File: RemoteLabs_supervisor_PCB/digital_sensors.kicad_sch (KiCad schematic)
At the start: 8 parts

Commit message: V1.0 Circuit Design Complete
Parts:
- gave numbers to parts that had none: 8
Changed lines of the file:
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@@
   (symbol (lib_id "000_Resistors_Immo:Resistor_0805") (at 128.27 99.06 0) (unit 1)
     (in_bom yes) (on_board yes) (fields_autoplaced)
-    (property "Reference" "R?" (id 0) (at 130.81 97.7899 0)
+    (property "Reference" "R21" (id 0) (at 130.81 97.7899 0)
       (effects (font (size 1.27 1.27)) (justify left))
     )
@@
   (symbol (lib_id "000_Resistors_Immo:Resistor_0805") (at 101.6 99.06 0) (unit 1)
     (in_bom yes) (on_board yes) (fields_autoplaced)
-    (property "Reference" "R?" (id 0) (at 104.14 97.7899 0)
+    (property "Reference" "R17" (id 0) (at 104.14 97.7899 0)
       (effects (font (size 1.27 1.27)) (justify left))
     )
@@
   (symbol (lib_id "000_Resistors_Immo:Resistor_0805") (at 118.11 38.1 0) (unit 1)
     (in_bom yes) (on_board yes) (fields_autoplaced)
-    (property "Reference" "R?" (id 0) (at 120.65 36.8299 0)
+    (property "Reference" "R20" (id 0) (at 120.65 36.8299 0)
       (effects (font (size 1.27 1.27)) (justify left))
     )
@@
   (symbol (lib_id "000_Resistors_Immo:Resistor_0805") (at 114.3 99.06 0) (unit 1)
     (in_bom yes) (on_board yes) (fields_autoplaced)
-    (property "Reference" "R?" (id 0) (at 116.84 97.7899 0)
+    (property "Reference" "R19" (id 0) (at 116.84 97.7899 0)
       (effects (font (size 1.27 1.27)) (justify left))
     )
@@
   (symbol (lib_id "Connector:Conn_01x02_Male") (at 87.63 45.72 0) (unit 1)
     (in_bom yes) (on_board yes) (fields_autoplaced)
-    (property "Reference" "J?" (id 0) (at 88.265 40.64 0))
+    (property "Reference" "J23" (id 0) (at 88.265 40.64 0))
     (property "Value" "limit_switch_A" (id 1) (at 88.265 43.18 0))
     (property "Footprint" "" (id 2) (at 87.63 45.72 0)
@@
   (symbol (lib_id "000_Pin_Headers_Immo:Conn_01x05_Male") (at 87.63 106.68 0) (mirror x) (unit 1)
     (in_bom yes) (on_board yes)
-    (property "Reference" "J?" (id 0) (at 78.74 95.25 0))
+    (property "Reference" "J25" (id 0) (at 78.74 95.25 0))
     (property "Value" "Optical Encoder" (id 1) (at 85.09 97.79 0))
     (property "Footprint" "Connector_PinHeader_1.27mm:PinHeader_1x05_P1.27mm_Vertical" (id 2) (at 87.63 106.68 0)
@@
   (symbol (lib_id "000_Resistors_Immo:Resistor_0805") (at 110.49 38.1 0) (unit 1)
     (in_bom yes) (on_board yes) (fields_autoplaced)
-    (property "Reference" "R?" (id 0) (at 113.03 36.8299 0)
+    (property "Reference" "R18" (id 0) (at 113.03 36.8299 0)
       (effects (font (size 1.27 1.27)) (justify left))
     )
@@
   (symbol (lib_id "Connector:Conn_01x02_Male") (at 87.63 55.88 0) (unit 1)
     (in_bom yes) (on_board yes) (fields_autoplaced)
-    (property "Reference" "J?" (id 0) (at 88.265 50.8 0))
+    (property "Reference" "J24" (id 0) (at 88.265 50.8 0))
     (property "Value" "limit_switch_B" (id 1) (at 88.265 53.34 0))
     (property "Footprint" "" (id 2) (at 87.63 55.88 0)

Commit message: Schematic reviewed
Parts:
- J23, J24: footprint (none) -> Connector_PinHeader_2.54mm:PinHeader_1x02_P2.54mm_Vertical
- J25: footprint Connector_PinHeader_1.27mm:PinHeader_1x05_P1.27mm_Vertical -> Connector_PinHeader_2.54mm:PinHeader_1x05_P2.54mm_Vertical
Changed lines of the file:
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@@
     (property "Reference" "J23" (id 0) (at 88.265 40.64 0))
     (property "Value" "limit_switch_A" (id 1) (at 88.265 43.18 0))
-    (property "Footprint" "" (id 2) (at 87.63 45.72 0)
+    (property "Footprint" "Connector_PinHeader_2.54mm:PinHeader_1x02_P2.54mm_Vertical" (id 2) (at 87.63 45.72 0)
       (effects (font (size 1.27 1.27)) hide)
     )
@@
     (property "Reference" "J25" (id 0) (at 78.74 95.25 0))
     (property "Value" "Optical Encoder" (id 1) (at 85.09 97.79 0))
-    (property "Footprint" "Connector_PinHeader_1.27mm:PinHeader_1x05_P1.27mm_Vertical" (id 2) (at 87.63 106.68 0)
+    (property "Footprint" "Connector_PinHeader_2.54mm:PinHeader_1x05_P2.54mm_Vertical" (id 2) (at 87.63 106.68 0)
       (effects (font (size 1.27 1.27)) hide)
     )
@@
     (pin "2")
   )
-  (symbol (lib_id "Connector:Conn_01x02_Male") (at 87.63 55.88 0) (unit 1)
+  (symbol (lib_name "Conn_01x02_Male_1") (lib_id "Connector:Conn_01x02_Male") (at 87.63 55.88 0) (unit 1)
     (in_bom yes) (on_board yes) (fields_autoplaced)
     (property "Reference" "J24" (id 0) (at 88.265 50.8 0))
     (property "Value" "limit_switch_B" (id 1) (at 88.265 53.34 0))
-    (property "Footprint" "" (id 2) (at 87.63 55.88 0)
+    (property "Footprint" "Connector_PinHeader_2.54mm:PinHeader_1x02_P2.54mm_Vertical" (id 2) (at 87.63 55.88 0)
       (effects (font (size 1.27 1.27)) hide)
     )

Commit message: mbncmvbc,
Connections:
- net LIMIT_SWITCH_A: now also R18.1; no longer R18.2
- net LIMIT_SWITCH_B: now also R20.1; no longer R20.2
- net OE_A: now also R17.1; no longer R17.2
- net OE_B: now also R21.1; no longer R21.2
- net OE_INDEX: now also R19.1; no longer R19.2
- net VCC: now also R17.2, R18.2, R19.2, R20.2, R21.2; no longer R17.1, R18.1, R19.1, R20.1, R21.1
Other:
- moved on the sheet: R17, R18, R19, R20, R21
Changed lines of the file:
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@@
     (effects (font (size 1.27 1.27)) (justify left))
   )
-  (symbol (lib_id "000_Resistors_Immo:Resistor_0805") (at 128.27 99.06 0) (unit 1)
+  (symbol (lib_id "000_Resistors_Immo:Resistor_0805") (at 128.27 99.06 90) (unit 1)
     (in_bom yes) (on_board yes) (fields_autoplaced)
-    (property "Reference" "R21" (id 0) (at 130.81 97.7899 0)
-      (effects (font (size 1.27 1.27)) (justify left))
+    (property "Reference" "R21" (id 0) (at 130.81 97.7899 90)
+      (effects (font (size 1.27 1.27)) (justify right))
     )
-    (property "Value" "2k7" (id 1) (at 130.81 100.3299 0)
-      (effects (font (size 1.27 1.27)) (justify left))
+    (property "Value" "2k7" (id 1) (at 130.81 100.3299 90)
+      (effects (font (size 1.27 1.27)) (justify right))
     )
-    (property "Footprint" "Resistor_SMD:R_0805_2012Metric_Pad1.20x1.40mm_HandSolder" (id 2) (at 126.492 99.06 90)
+    (property "Footprint" "Resistor_SMD:R_0805_2012Metric_Pad1.20x1.40mm_HandSolder" (id 2) (at 128.27 100.838 90)
       (effects (font (size 1.27 1.27)) hide)
     )
@@
     (pin "2")
   )
-  (symbol (lib_id "000_Resistors_Immo:Resistor_0805") (at 101.6 99.06 0) (unit 1)
+  (symbol (lib_id "000_Resistors_Immo:Resistor_0805") (at 101.6 99.06 90) (unit 1)
     (in_bom yes) (on_board yes) (fields_autoplaced)
-    (property "Reference" "R17" (id 0) (at 104.14 97.7899 0)
-      (effects (font (size 1.27 1.27)) (justify left))
+    (property "Reference" "R17" (id 0) (at 104.14 97.7899 90)
+      (effects (font (size 1.27 1.27)) (justify right))
     )
-    (property "Value" "2k7" (id 1) (at 104.14 100.3299 0)
-      (effects (font (size 1.27 1.27)) (justify left))
+    (property "Value" "2k7" (id 1) (at 104.14 100.3299 90)
+      (effects (font (size 1.27 1.27)) (justify right))
     )
-    (property "Footprint" "Resistor_SMD:R_0805_2012Metric_Pad1.20x1.40mm_HandSolder" (id 2) (at 99.822 99.06 90)
+    (property "Footprint" "Resistor_SMD:R_0805_2012Metric_Pad1.20x1.40mm_HandSolder" (id 2) (at 101.6 100.838 90)
       (effects (font (size 1.27 1.27)) hide)
     )
@@
     (pin "2")
   )
-  (symbol (lib_id "000_Resistors_Immo:Resistor_0805") (at 118.11 38.1 0) (unit 1)
+  (symbol (lib_id "000_Resistors_Immo:Resistor_0805") (at 118.11 38.1 90) (unit 1)
     (in_bom yes) (on_board yes) (fields_autoplaced)
-    (property "Reference" "R20" (id 0) (at 120.65 36.8299 0)
-      (effects (font (size 1.27 1.27)) (justify left))
+    (property "Reference" "R20" (id 0) (at 120.65 36.8299 90)
+      (effects (font (size 1.27 1.27)) (justify right))
     )
-    (property "Value" "10k" (id 1) (at 120.65 39.3699 0)
-      (effects (font (size 1.27 1.27)) (justify left))
+    (property "Value" "10k" (id 1) (at 120.65 39.3699 90)
+      (effects (font (size 1.27 1.27)) (justify right))
     )
-    (property "Footprint" "Resistor_SMD:R_0805_2012Metric_Pad1.20x1.40mm_HandSolder" (id 2) (at 116.332 38.1 90)
+    (property "Footprint" "Resistor_SMD:R_0805_2012Metric_Pad1.20x1.40mm_HandSolder" (id 2) (at 118.11 39.878 90)
       (effects (font (size 1.27 1.27)) hide)
     )
@@
     (pin "2")
   )
-  (symbol (lib_id "000_Resistors_Immo:Resistor_0805") (at 114.3 99.06 0) (unit 1)
+  (symbol (lib_id "000_Resistors_Immo:Resistor_0805") (at 114.3 99.06 90) (unit 1)
     (in_bom yes) (on_board yes) (fields_autoplaced)
-    (property "Reference" "R19" (id 0) (at 116.84 97.7899 0)
-      (effects (font (size 1.27 1.27)) (justify left))
+    (property "Reference" "R19" (id 0) (at 116.84 97.7899 90)
+      (effects (font (size 1.27 1.27)) (justify right))
     )
-    (property "Value" "2k7" (id 1) (at 116.84 100.3299 0)
-      (effects (font (size 1.27 1.27)) (justify left))
+    (property "Value" "2k7" (id 1) (at 116.84 100.3299 90)
+      (effects (font (size 1.27 1.27)) (justify right))
     )
-    (property "Footprint" "Resistor_SMD:R_0805_2012Metric_Pad1.20x1.40mm_HandSolder" (id 2) (at 112.522 99.06 90)
+    (property "Footprint" "Resistor_SMD:R_0805_2012Metric_Pad1.20x1.40mm_HandSolder" (id 2) (at 114.3 100.838 90)
       (effects (font (size 1.27 1.27)) hide)
     )
@@
     (pin "5")
   )
-  (symbol (lib_id "000_Resistors_Immo:Resistor_0805") (at 110.49 38.1 0) (unit 1)
+  (symbol (lib_id "000_Resistors_Immo:Resistor_0805") (at 110.49 38.1 90) (unit 1)
     (in_bom yes) (on_board yes) (fields_autoplaced)
-    (property "Reference" "R18" (id 0) (at 113.03 36.8299 0)
-      (effects (font (size 1.27 1.27)) (justify left))
+    (property "Reference" "R18" (id 0) (at 113.03 36.8299 90)
+      (effects (font (size 1.27 1.27)) (justify right))
     )
-    (property "Value" "10k" (id 1) (at 113.03 39.3699 0)
-      (effects (font (size 1.27 1.27)) (justify left))
+    (property "Value" "10k" (id 1) (at 113.03 39.3699 90)
+      (effects (font (size 1.27 1.27)) (justify right))
     )
-    (property "Footprint" "Resistor_SMD:R_0805_2012Metric_Pad1.20x1.40mm_HandSolder" (id 2) (at 108.712 38.1 90)
+    (property "Footprint" "Resistor_SMD:R_0805_2012Metric_Pad1.20x1.40mm_HandSolder" (id 2) (at 110.49 39.878 90)
       (effects (font (size 1.27 1.27)) hide)
     )
@@
     (pin "2")
   )
-  (symbol (lib_name "Conn_01x02_Male_1") (lib_id "Connector:Conn_01x02_Male") (at 87.63 55.88 0) (unit 1)
+  (symbol (lib_id "Connector:Conn_01x02_Male") (at 87.63 55.88 0) (unit 1)
     (in_bom yes) (on_board yes) (fields_autoplaced)
     (property "Reference" "J24" (id 0) (at 88.265 50.8 0))

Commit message: PCB layout
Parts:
- J23, J24: footprint Connector_PinHeader_2.54mm:PinHeader_1x02_P2.54mm_Vertical -> Connector_Molex:Molex_KK-254_AE-6410-02A_1x02_P2.54mm_Vertical; symbol Connector:Conn_01x02_Male -> 000_Connectors_Immo:2pin_molex_2.54mm_male
- J25: footprint Connector_PinHeader_2.54mm:PinHeader_1x05_P2.54mm_Vertical -> Connector_Molex:Molex_KK-254_AE-6410-05A_1x05_P2.54mm_Vertical; symbol 000_Pin_Headers_Immo:Conn_01x05_Male -> 000_Pin_Headers_Immo:Molex_5pin_2.54mm_M
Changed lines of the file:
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@@
     (pin "2")
   )
-  (symbol (lib_id "Connector:Conn_01x02_Male") (at 87.63 45.72 0) (unit 1)
+  (symbol (lib_id "000_Connectors_Immo:2pin_molex_2.54mm_male") (at 87.63 45.72 0) (unit 1)
     (in_bom yes) (on_board yes) (fields_autoplaced)
     (property "Reference" "J23" (id 0) (at 88.265 40.64 0))
     (property "Value" "limit_switch_A" (id 1) (at 88.265 43.18 0))
-    (property "Footprint" "Connector_PinHeader_2.54mm:PinHeader_1x02_P2.54mm_Vertical" (id 2) (at 87.63 45.72 0)
+    (property "Footprint" "Connector_Molex:Molex_KK-254_AE-6410-02A_1x02_P2.54mm_Vertical" (id 2) (at 87.63 45.72 0)
       (effects (font (size 1.27 1.27)) hide)
     )
@@
     (pin "2")
   )
-  (symbol (lib_id "000_Pin_Headers_Immo:Conn_01x05_Male") (at 87.63 106.68 0) (mirror x) (unit 1)
+  (symbol (lib_id "000_Pin_Headers_Immo:Molex_5pin_2.54mm_M") (at 87.63 106.68 0) (mirror x) (unit 1)
     (in_bom yes) (on_board yes)
     (property "Reference" "J25" (id 0) (at 78.74 95.25 0))
     (property "Value" "Optical Encoder" (id 1) (at 85.09 97.79 0))
-    (property "Footprint" "Connector_PinHeader_2.54mm:PinHeader_1x05_P2.54mm_Vertical" (id 2) (at 87.63 106.68 0)
+    (property "Footprint" "Connector_Molex:Molex_KK-254_AE-6410-05A_1x05_P2.54mm_Vertical" (id 2) (at 89.535 96.52 0)
       (effects (font (size 1.27 1.27)) hide)
     )
@@
     (pin "2")
   )
-  (symbol (lib_id "Connector:Conn_01x02_Male") (at 87.63 55.88 0) (unit 1)
+  (symbol (lib_id "000_Connectors_Immo:2pin_molex_2.54mm_male") (at 87.63 55.88 0) (unit 1)
     (in_bom yes) (on_board yes) (fields_autoplaced)
     (property "Reference" "J24" (id 0) (at 88.265 50.8 0))
     (property "Value" "limit_switch_B" (id 1) (at 88.265 53.34 0))
-    (property "Footprint" "Connector_PinHeader_2.54mm:PinHeader_1x02_P2.54mm_Vertical" (id 2) (at 87.63 55.88 0)
+    (property "Footprint" "Connector_Molex:Molex_KK-254_AE-6410-02A_1x02_P2.54mm_Vertical" (id 2) (at 87.63 55.88 0)
       (effects (font (size 1.27 1.27)) hide)
     )

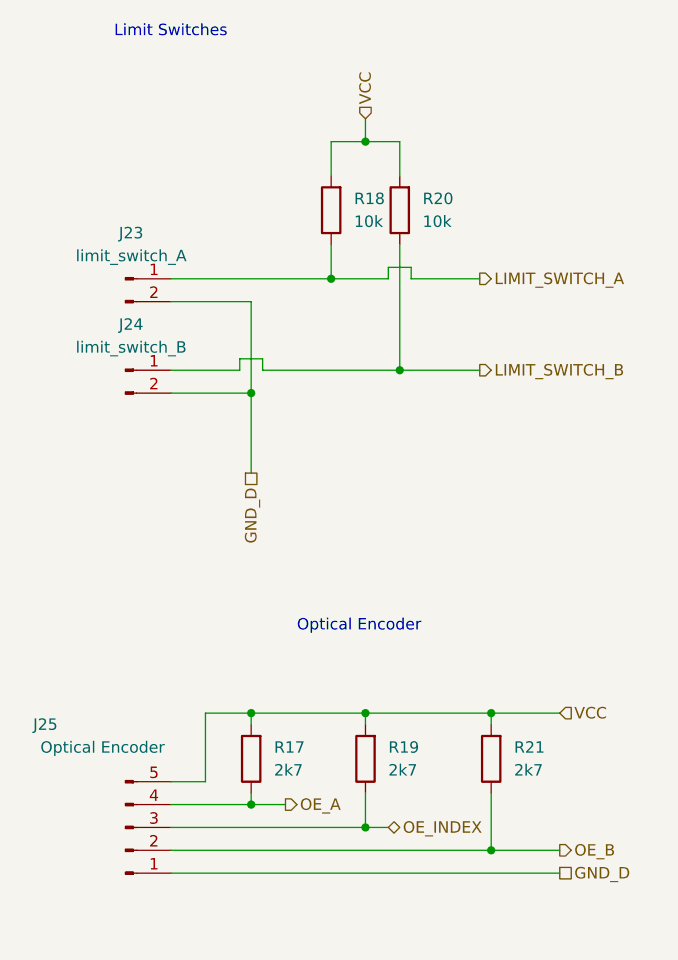
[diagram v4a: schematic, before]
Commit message: Test software mostly tested - awaiting hardware
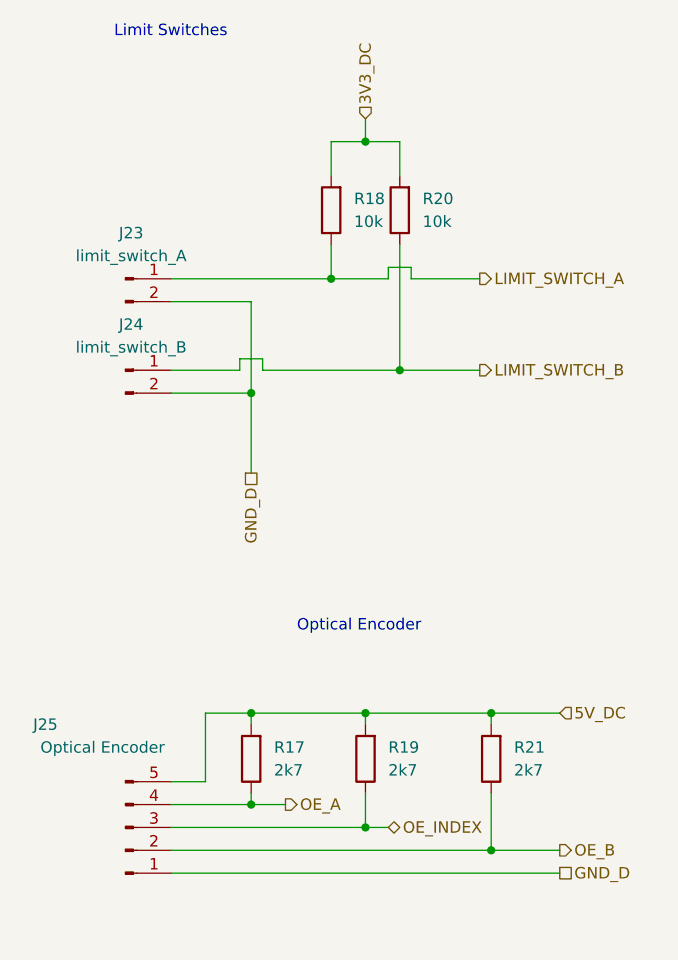
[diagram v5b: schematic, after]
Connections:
- net VCC renamed 5V_DC
- net 5V_DC: no longer R18.2, R20.2
- new net 3V3_DC: R18.2, R20.2
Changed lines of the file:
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@@
     (effects (font (size 1.27 1.27)) (justify left bottom))
   )
-  (hierarchical_label "VCC" (shape input) (at 114.3 27.94 90)
+  (hierarchical_label "3V3_DC" (shape input) (at 114.3 27.94 90)
     (effects (font (size 1.27 1.27)) (justify left))
   )
@@
     (effects (font (size 1.27 1.27)) (justify left))
   )
-  (hierarchical_label "VCC" (shape input) (at 135.89 93.98 0)
+  (hierarchical_label "5V_DC" (shape input) (at 135.89 93.98 0)
     (effects (font (size 1.27 1.27)) (justify left))
   )

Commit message: Edited PCB design for V1.1
- Changed pin sizes for stepper motor
- Change pin sizes for DC/DC Buck module.
- In process of changing text to be readable by human beings
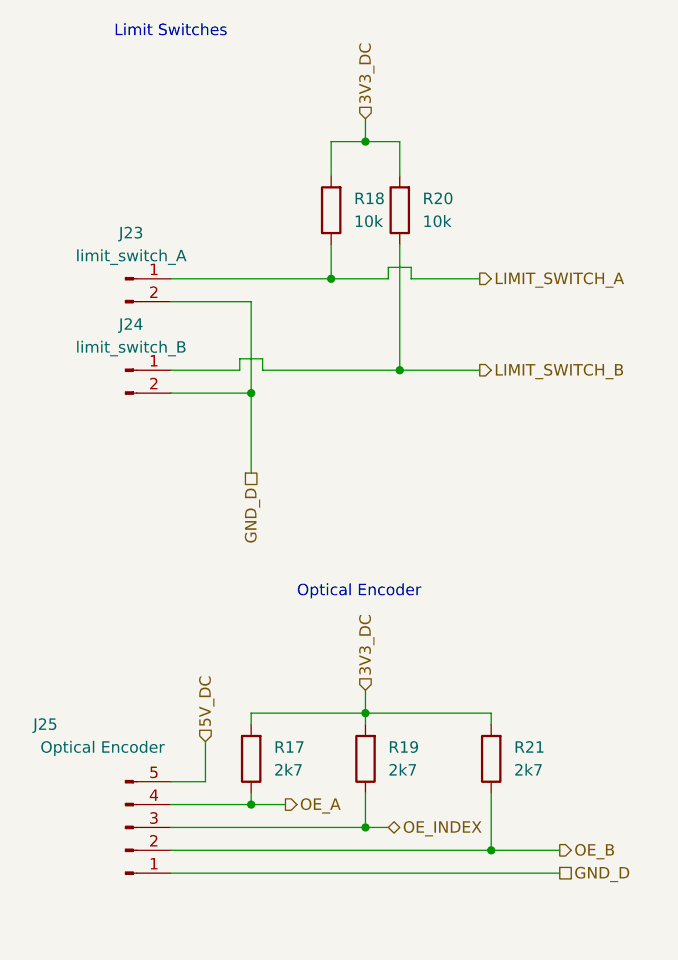
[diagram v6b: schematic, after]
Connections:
- net 3V3_DC: now also R17.2, R19.2, R21.2
- net 5V_DC: no longer R17.2, R19.2, R21.2
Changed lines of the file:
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@@
   (junction (at 101.6 58.42) (diameter 0) (color 0 0 0 0)
   )
-  (junction (at 128.27 93.98) (diameter 0) (color 0 0 0 0)
+  (junction (at 114.3 93.98) (diameter 0) (color 0 0 0 0)
   )
   (junction (at 114.3 106.68) (diameter 0) (color 0 0 0 0)
-  )
-  (junction (at 101.6 93.98) (diameter 0) (color 0 0 0 0)
   )
   (junction (at 101.6 104.14) (diameter 0) (color 0 0 0 0)
@@
   (junction (at 114.3 30.48) (diameter 0) (color 0 0 0 0)
   )
-  (junction (at 114.3 93.98) (diameter 0) (color 0 0 0 0)
+  (wire (pts (xy 101.6 93.98) (xy 114.3 93.98))
+    (stroke (width 0) (type default) (color 0 0 0 0))
   )
   (wire (pts (xy 110.49 30.48) (xy 110.49 34.29))
@@
     (stroke (width 0) (type default) (color 0 0 0 0))
   )
+  (wire (pts (xy 128.27 93.98) (xy 128.27 95.25))
+    (stroke (width 0) (type default) (color 0 0 0 0))
+  )
   (wire (pts (xy 114.3 102.87) (xy 114.3 106.68))
     (stroke (width 0) (type default) (color 0 0 0 0))
   )
   (wire (pts (xy 101.6 58.42) (xy 101.6 67.31))
+    (stroke (width 0) (type default) (color 0 0 0 0))
+  )
+  (wire (pts (xy 101.6 95.25) (xy 101.6 93.98))
     (stroke (width 0) (type default) (color 0 0 0 0))
   )
@@
     (stroke (width 0) (type default) (color 0 0 0 0))
   )
+  (wire (pts (xy 96.52 97.155) (xy 96.52 101.6))
+    (stroke (width 0) (type default) (color 0 0 0 0))
+  )
   (wire (pts (xy 118.11 30.48) (xy 118.11 34.29))
     (stroke (width 0) (type default) (color 0 0 0 0))
   )
   (wire (pts (xy 92.71 111.76) (xy 135.89 111.76))
-    (stroke (width 0) (type default) (color 0 0 0 0))
-  )
-  (wire (pts (xy 114.3 93.98) (xy 114.3 95.25))
-    (stroke (width 0) (type default) (color 0 0 0 0))
-  )
-  (wire (pts (xy 101.6 93.98) (xy 114.3 93.98))
     (stroke (width 0) (type default) (color 0 0 0 0))
   )
@@
     (stroke (width 0) (type default) (color 0 0 0 0))
   )
-  (wire (pts (xy 101.6 93.98) (xy 101.6 95.25))
-    (stroke (width 0) (type default) (color 0 0 0 0))
-  )
   (wire (pts (xy 92.71 48.26) (xy 101.6 48.26))
     (stroke (width 0) (type default) (color 0 0 0 0))
   )
-  (wire (pts (xy 96.52 101.6) (xy 96.52 93.98))
-    (stroke (width 0) (type default) (color 0 0 0 0))
-  )
-  (wire (pts (xy 128.27 93.98) (xy 128.27 95.25))
+  (wire (pts (xy 114.3 91.44) (xy 114.3 93.98))
     (stroke (width 0) (type default) (color 0 0 0 0))
   )
@@
     (stroke (width 0) (type default) (color 0 0 0 0))
   )
-  (wire (pts (xy 96.52 93.98) (xy 101.6 93.98))
+  (wire (pts (xy 114.3 93.98) (xy 114.3 95.25))
     (stroke (width 0) (type default) (color 0 0 0 0))
   )
   (wire (pts (xy 118.11 55.88) (xy 127 55.88))
-    (stroke (width 0) (type default) (color 0 0 0 0))
-  )
-  (wire (pts (xy 128.27 93.98) (xy 135.89 93.98))
     (stroke (width 0) (type default) (color 0 0 0 0))
   )
@@
     (stroke (width 0) (type default) (color 0 0 0 0))
   )
-  (text "Optical Encoder" (at 106.68 85.09 0)
+  (text "Optical Encoder" (at 106.68 81.28 0)
     (effects (font (size 1.27 1.27)) (justify left bottom))
   )
@@
     (effects (font (size 1.27 1.27)) (justify left))
   )
-  (hierarchical_label "5V_DC" (shape input) (at 135.89 93.98 0)
+  (hierarchical_label "3V3_DC" (shape input) (at 114.3 91.44 90)
     (effects (font (size 1.27 1.27)) (justify left))
   )
+  (hierarchical_label "5V_DC" (shape input) (at 96.52 97.155 90)
+    (effects (font (size 1.27 1.27)) (justify left))
+  )
